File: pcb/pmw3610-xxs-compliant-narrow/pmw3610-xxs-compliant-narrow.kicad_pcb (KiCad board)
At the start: 2 copper layers, 16 x 25 mm, 14 parts, among them J2 vik-module-connector, U1 MCP1700T-1802E/TT, U2 PMW3610

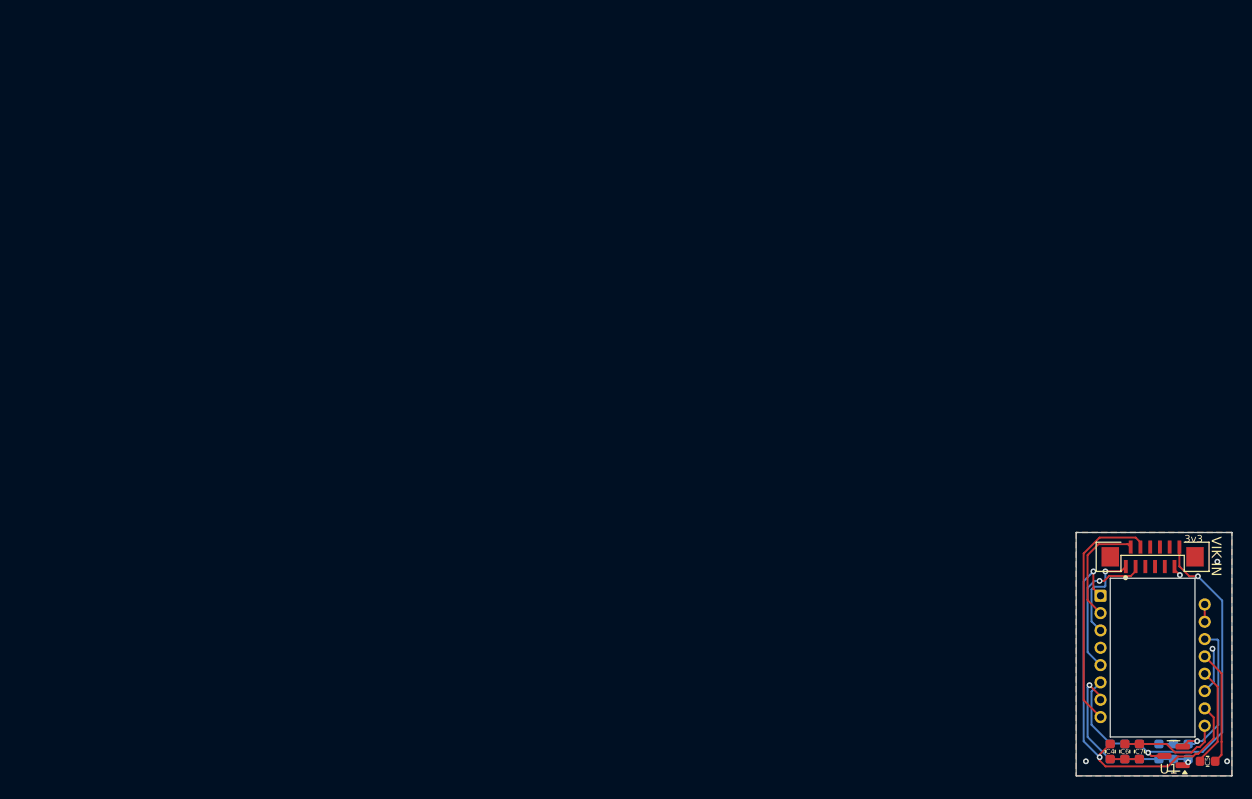
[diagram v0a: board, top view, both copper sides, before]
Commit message: Make PMW-3610-narrow module compliant with VIK small form factor.
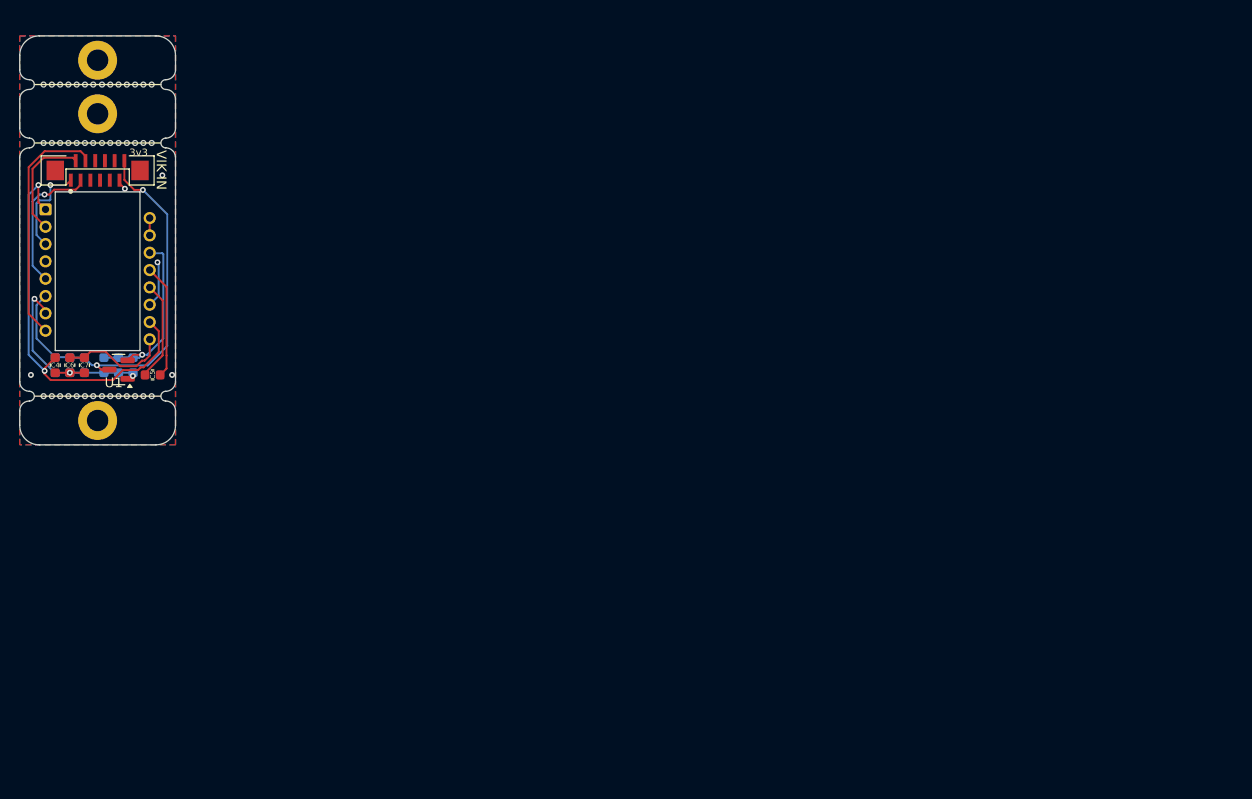
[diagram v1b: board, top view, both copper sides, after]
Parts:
- added REF**: MountingHole_2.2mm_M2_Pad, MountingHole:MountingHole_2.2mm_M2_Pad, F.Cu at (28.0, 28.0)
- added REF**: BreakLine_7h_D0.5mm_P0.85mm, Panelization:BreakLine_7h_D0.5mm_P0.85mm, F.Cu at (31.0, 25.0)
- added REF**: BreakLine_7h_D0.5mm_P0.85mm, Panelization:BreakLine_7h_D0.5mm_P0.85mm, F.Cu at (25.0, 31.0)
- added REF**: MountingHole_2.2mm_M2_Pad, MountingHole:MountingHole_2.2mm_M2_Pad, F.Cu at (28.0, 59.5)
- added REF**: BreakLine_7h_D0.5mm_P0.85mm, Panelization:BreakLine_7h_D0.5mm_P0.85mm, F.Cu at (25.0, 57.0)
- added REF**: BreakLine_7h_D0.5mm_P0.85mm, Panelization:BreakLine_7h_D0.5mm_P0.85mm, F.Cu at (25.0, 25.0)
- added REF**: MountingHole_2.2mm_M2_Pad, MountingHole:MountingHole_2.2mm_M2_Pad, F.Cu at (28.0, 22.5)
- added REF**: BreakLine_7h_D0.5mm_P0.85mm, Panelization:BreakLine_7h_D0.5mm_P0.85mm, F.Cu at (31.0, 57.0)
- added REF**: BreakLine_7h_D0.5mm_P0.85mm, Panelization:BreakLine_7h_D0.5mm_P0.85mm, F.Cu at (31.0, 31.0)
- moved C1 115.4 mm to (26.6, 53.8)
- moved C2 115.4 mm to (28.6, 53.8)
- moved C3 115.4 mm to (25.1, 53.8)
- moved C4 115.4 mm to (23.6, 53.8)
- moved C5 115.4 mm to (33.6, 54.8)
- moved C6 115.4 mm to (25.1, 53.8)
- moved C7 115.4 mm to (26.6, 53.8)
- moved C8 115.4 mm to (31.6, 53.8)
- moved C9 115.4 mm to (30.1, 53.8)
- moved J2 115.4 mm to (28.0, 33.8)
- moved R1 115.4 mm to (23.6, 53.8)
- moved REF** 115.4 mm to (33.6, 34.3)
- moved U1 115.4 mm to (30.1, 54.3)
- moved U2 115.4 mm to (28.0, 44.0)
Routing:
- net Net-(U2-VCP): track 10.7 -> 11.2 mm
- net GND: vias 6 -> 7
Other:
- board size 16 x 25 mm -> 16 x 42 mm

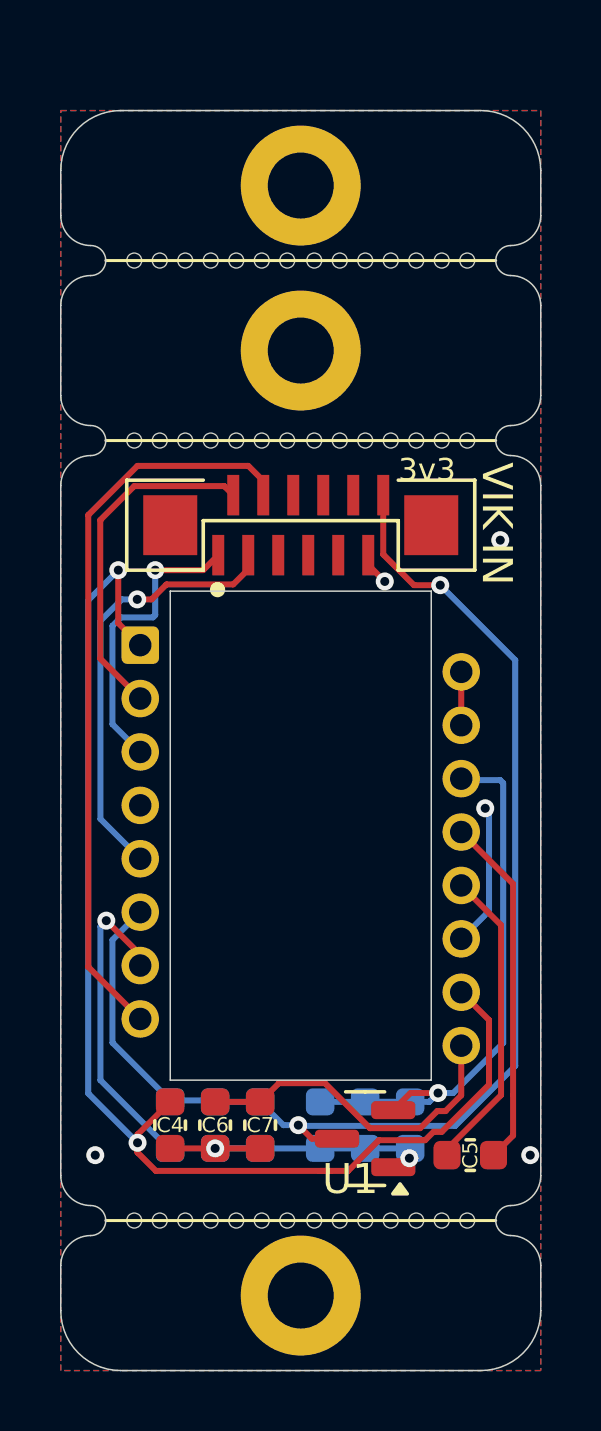
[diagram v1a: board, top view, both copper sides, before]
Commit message: Change VIK connector on trackball sensor module.
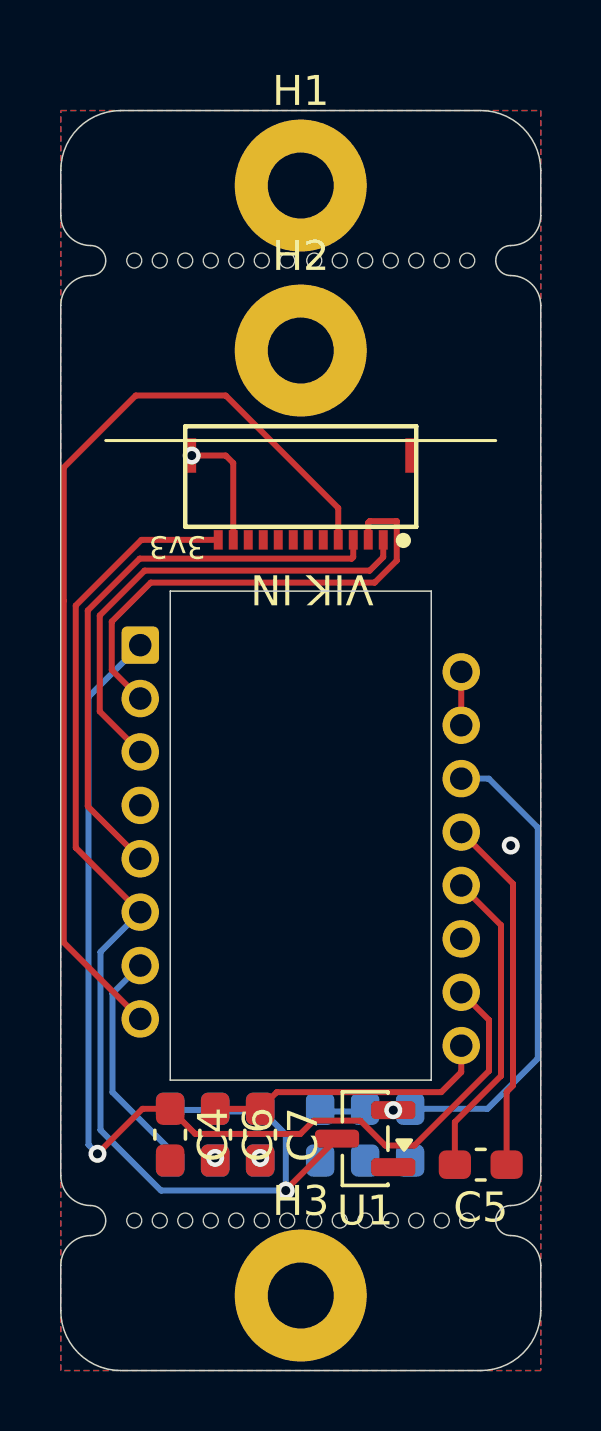
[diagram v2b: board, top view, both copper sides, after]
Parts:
- removed the REF** at (28.0, 28.0)
- removed the REF** at (25.0, 31.0)
- removed the REF** at (28.0, 59.5)
- removed the REF** at (28.0, 22.5)
- removed the REF** at (31.0, 31.0)
- added H1: MountingHole_Pad, MountingHole:MountingHole_2.2mm_M2_Pad, F.Cu at (28.0, 22.5)
- added H2: MountingHole_Pad, MountingHole:MountingHole_2.2mm_M2_Pad, F.Cu at (28.0, 28.0)
- added H3: MountingHole_Pad, MountingHole:MountingHole_2.2mm_M2_Pad, F.Cu at (28.0, 59.5)
- C1, C2, C3, C4, C5, C6, C7, C8, C9: footprint roBa:C_0603_1608Metric -> Capacitor_SMD:C_0603_1608Metric_Pad1.08x0.95mm_HandSolder
- J2: footprint vik:vik-module-connector-vertical -> vik:vik-module-connector-horizontal-mini
- R1: footprint roBa:R_0603_1608Metric -> Resistor_SMD:R_0603_1608Metric_Pad0.98x0.95mm_HandSolder
- U1: footprint roBa:SOT-23 -> Package_TO_SOT_SMD:SOT-23
- moved J2 1.62 mm to (28.0, 32.2), turned to 180 degrees
- moved C5 0.47 mm to (34.0, 55.1)
- moved C1 0.32 mm to (26.6, 54.1)
- moved C2 0.32 mm to (28.6, 54.1)
- moved C3 0.32 mm to (25.1, 54.1)
- moved C4 0.32 mm to (23.6, 54.1)
- moved C6 0.32 mm to (25.1, 54.1)
- moved C7 0.32 mm to (26.6, 54.1)
- moved C8 0.32 mm to (31.6, 54.1)
- moved C9 0.32 mm to (30.1, 54.1)
- moved R1 0.32 mm to (23.6, 54.1)
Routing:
- net GND: track 16.1 -> 4.05 mm, vias 7 -> 4
- net MOTION: track 24.7 -> 32.2 mm
- net Net-(U2-+VCSEL): track 42.5 -> 36.4 mm, vias 2 -> 1
- net SCLK: track 9.97 -> 15.9 mm, vias 1 -> 0
- net SDIO: track 11.5 -> 16.2 mm
- net NCS: track 14.6 -> 19.2 mm, vias 1 -> 0
- net Net-(U2-NRESET): track 10.7 -> 7.32 mm, vias 1 -> 0
- net VCC: track 43.1 -> 40.2 mm, vias 2 -> 1
- net +1V9: track 20.9 -> 18.9 mm
- net Net-(U2-VCP): track 11.2 -> 9.59 mm
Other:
- outline, holes or cut-outs redrawn
